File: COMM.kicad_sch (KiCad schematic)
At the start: 6 parts

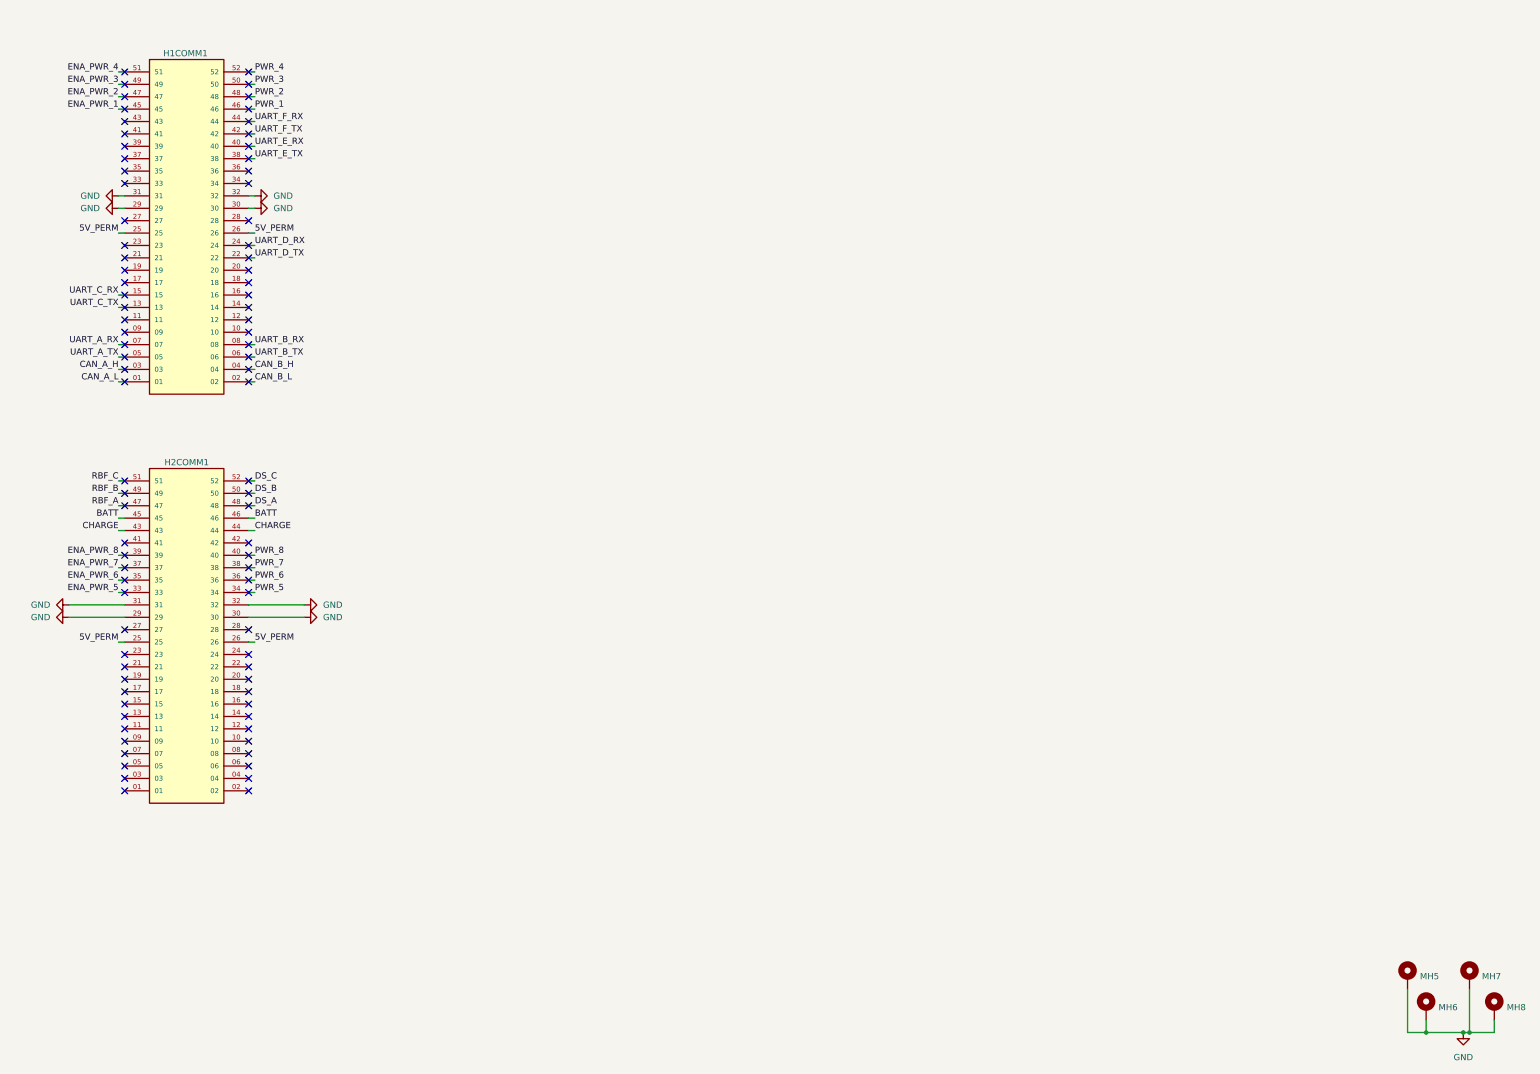
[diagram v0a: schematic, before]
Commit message: Updated COMM board
Includes: Xbee, RPico, TCAN, RS485
As of 12/5/2025
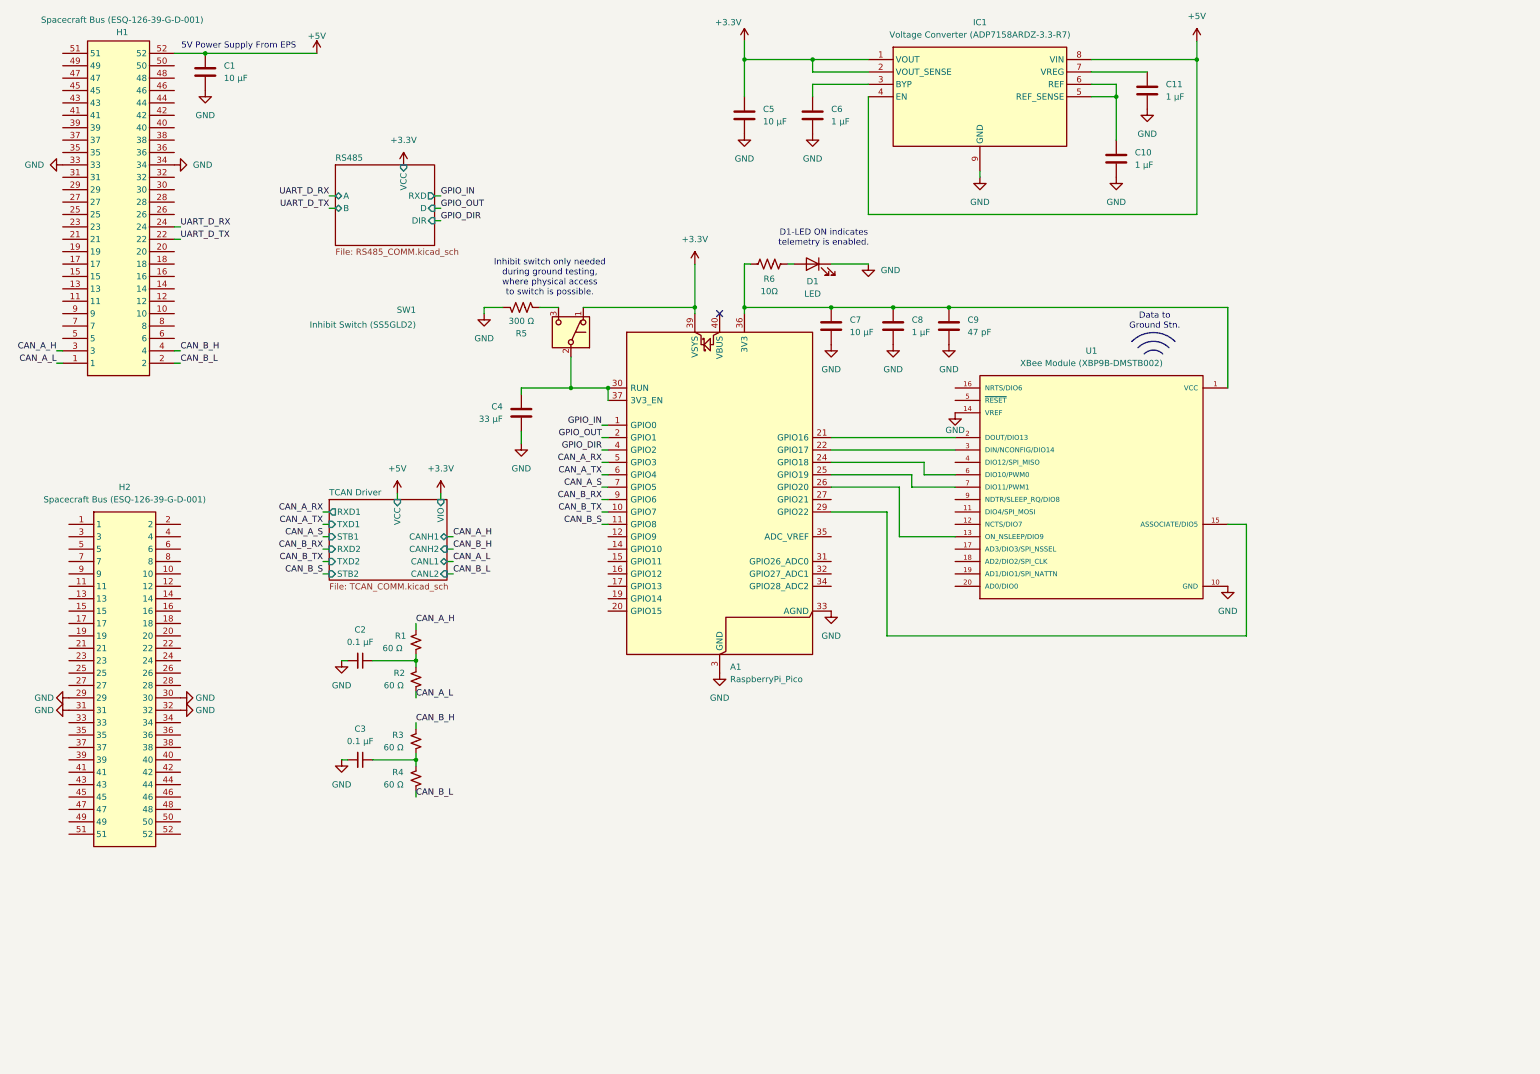
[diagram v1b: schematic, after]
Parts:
- removed H1COMM1, H2COMM1: Conn_02x26_Odd_Even, ESQ-126-39-G-D:SAMTEC_ESQ-126-39-G-D, symbol ESQ-126-39-G-D:ESQ-126-39-G-D
- removed MH5, MH6, MH7, MH8: MountingHole_Pad, MountingHole:MountingHole_3.2mm_M3_Pad_Via, symbol Mechanical:MountingHole_Pad
- added A1: RaspberryPi_Pico, Module:RaspberryPi_Pico_Common_THT, symbol MCU_Module:RaspberryPi_Pico
- added C1, C5, C7: 10 μF, C_10uF:CAPC1005X70N, symbol Device:C
- added C10, C11, C6, C8: 1 μF, C_1uF:CAPC1005X55N, symbol Device:C
- added C2, C3: 0.1 μF, Capacitor_SMD:C_0805_2012Metric, symbol Device:C_Small
- added C4: 33 µF, C3216X5R1C336M160AB:CAPC3216X180N, symbol Device:C
- added C9: 47 pF, C_47pF:CAPC1005X55N, symbol Device:C
- added D1: LED, LED_THT:LED_D5.0mm, symbol Device:LED
- added H1, H2: Spacecraft Bus (ESQ-126-39-G-D-001), SpaceBus:RHDR52W64P254_2X26_6654X495X1135P, symbol ESQ-126-39-G-D-001:ESQ-126-39-G-D-001
- added IC1: Voltage Converter (ADP7158ARDZ-3.3-R7), Voltage Converter 5Vto3.3V:SOIC127P600X175-9N, symbol ADP7158ARDZ-3_3-R7:ADP7158ARDZ-3.3-R7
- added R1, R2, R3, R4: 60 Ω, Resistor_SMD:R_0805_2012Metric, symbol Device:R_Small_US
- added R5: 300 Ω, Resistor_SMD:R_0805_2012Metric, symbol Device:R_US
- added R6: 10Ω, R_10OHM:RESC1005X40, symbol Device:R_US
- added SW1: Inhibit Switch (SS5GLD2), Inhibit_Switch_COMM:SS5GLD2, symbol Switch:SW_Push_SPDT
- added U1: XBee Module (XBP9B-DMSTB002), XBP9B-DMSTB002:DIP2200W51P200L3294H279Q20P, symbol XBP9B-DMSTB002:XBP9B-DMSTB002
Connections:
- net CAN_A_H: now also H1.3, R1.1
- net CAN_A_L: now also H1.1, R2.2
- net CAN_B_H: now also H1.4, R3.1
- net CAN_B_L: now also H1.2, R4.2
- net GND: now also A1.13 (GND), A1.18 (GND), A1.23 (GND), A1.28 (GND), A1.3 (GND), A1.33 (AGND), A1.38 (GND), A1.8 (GND), C1.2, C10.2, C11.2, C2.2, C3.2, C4.1, C5.2, C6.2, C7.2, C8.2, C9.2, D1.1 (K), H1.33, H1.34, H2.29, H2.30, H2.31, H2.32, IC1.9 (GND), R5.1, U1.10 (GND), U1.14 (VREF)
- net UART_D_RX: now also H1.24
- net UART_D_TX: now also H1.22
- new net: C3.1, R3.2, R4.1
- new net: C6.1, IC1.3 (BYP)
- new net: C11.1, IC1.7 (VREG)
- new net: A1.36 (3V3), C7.1, C8.1, C9.1, R6.2, U1.1 (VCC)
- new net: A1.26 (GPIO20), U1.13 (ON_NSLEEP/DIO9)
- new net: A1.29 (GPIO22), U1.15 (ASSOCIATE/DIO5)
- new net: A1.21 (GPIO16), U1.2 (DOUT/DIO13)
- new net: A1.22 (GPIO17), U1.3 (DIN/NCONFIG/DIO14)
- new net: A1.24 (GPIO18), U1.6 (DIO10/PWM0)
- new net: A1.25 (GPIO19), U1.7 (DIO11/PWM1)
- new net: A1.30 (RUN), A1.37 (3V3_EN), C4.2, SW1.2 (B)
- new net: D1.2 (A), R6.1
- new net: C2.1, R1.2, R2.1
- new net: R5.2, SW1.3 (C)
- new net: C10.1, IC1.5 (REF_SENSE), IC1.6 (REF)
- new net +3.3V: A1.39 (VSYS), C5.1, IC1.1 (VOUT), IC1.2 (VOUT_SENSE), SW1.1 (A)
- new net +5V: C1.1, H1.52, IC1.4 (EN), IC1.8 (VIN)
- new net CAN_A_RX: A1.5 (GPIO3)
- new net CAN_A_S: A1.7 (GPIO5)
- new net CAN_A_TX: A1.6 (GPIO4)
- new net CAN_B_RX: A1.9 (GPIO6)
- new net CAN_B_S: A1.11 (GPIO8)
- new net CAN_B_TX: A1.10 (GPIO7)
- new net GPIO_DIR: A1.4 (GPIO2)
- new net GPIO_IN: A1.1 (GPIO0)
- new net GPIO_OUT: A1.2 (GPIO1)
- no-connect marks 88 -> 1
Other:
- added sheet RS485 (RS485_COMM.kicad_sch)
- added sheet TCAN Driver (TCAN_COMM.kicad_sch)
- note added: "5V Power Supply From EPS"
- note added: "D1-LED ON indicates telemetry is enabled."
- note added: "Data to Ground Stn."
- note added: "Inhibit switch only needed during ground testing, where physical access to switch is possible."
- company: University of Virginia -> (none)
- title: HEDGE2 Avionics -> (none)
